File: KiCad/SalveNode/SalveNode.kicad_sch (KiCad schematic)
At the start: 19 parts, among them IC2 TMP75AQDGKRQ1, IC3 DS89C21TMX_NOPB, IC3 VEML7700-TR, J1 Screw_Terminal_01x06, J21 Screw_Terminal_01x06, U1 ATmega328PB-A, Y1 Crystal

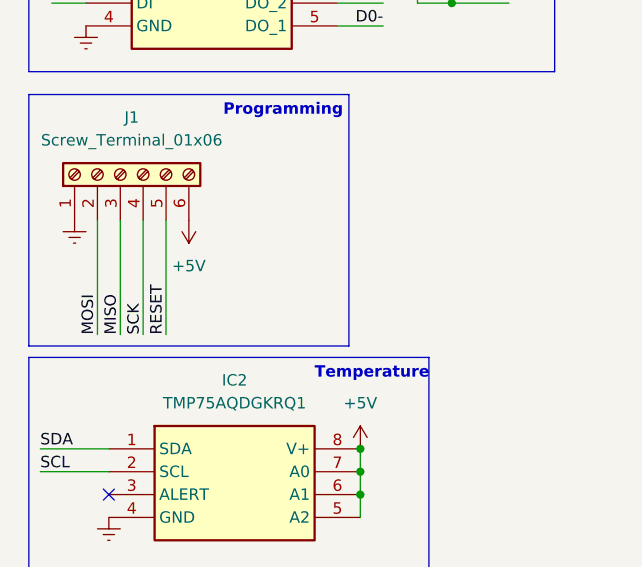
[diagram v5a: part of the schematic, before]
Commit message: fixed missing R for reset while programming
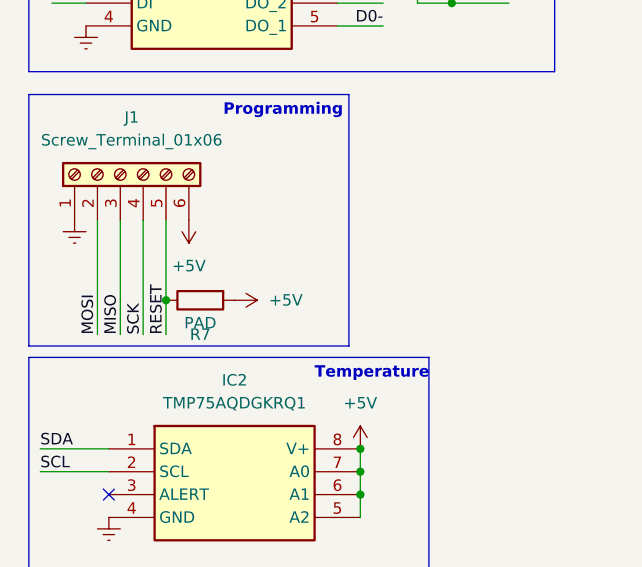
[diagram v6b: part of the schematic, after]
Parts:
- added R7: PAD, Resistor_SMD:R_1206_3216Metric_Pad1.30x1.75mm_HandSolder, symbol Device:R
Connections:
- net +5V: now also R7.2
- net RESET: now also R7.1
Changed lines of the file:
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@@
   (junction (at 156.21 27.94) (diameter 0) (color 0 0 0 0)
+  )
+  (junction (at 30.48 92.71) (diameter 0) (color 0 0 0 0)
   )
   (junction (at 181.61 27.94) (diameter 0) (color 0 0 0 0)
@@
     (stroke (width 0) (type default))
   )
-  (wire (pts (xy 30.48 83.82) (xy 30.48 96.52))
+  (wire (pts (xy 30.48 83.82) (xy 30.48 92.71))
     (stroke (width 0) (type default))
   )
@@
   )
   (wire (pts (xy 25.4 83.82) (xy 25.4 96.52))
+    (stroke (width 0) (type default))
+  )
+  (wire (pts (xy 30.48 92.71) (xy 30.48 96.52))
     (stroke (width 0) (type default))
   )
@@
     )
   )
+  (symbol (lib_id "Device:R") (at 34.29 92.71 90) (mirror x) (unit 1)
+    (in_bom yes) (on_board yes) (dnp no)
+    (property "Reference" "R7" (at 34.29 96.52 90)
+      (effects (font (size 1.27 1.27)))
+    )
+    (property "Value" "PAD" (at 34.29 95.25 90)
+      (effects (font (size 1.27 1.27)))
+    )
+    (property "Footprint" "Resistor_SMD:R_1206_3216Metric_Pad1.30x1.75mm_HandSolder" (at 34.29 90.932 90)
+      (effects (font (size 1.27 1.27)) hide)
+    )
+    (property "Datasheet" "~" (at 34.29 92.71 0)
+      (effects (font (size 1.27 1.27)) hide)
+    )
+    (pin "1")
+    (pin "2")
+    (instances
+      (project "KiCad"
+        (path "/557850ac-a946-4dff-8187-8978353577df"
+          (reference "R7") (unit 1)
+        )
+      )
+      (project "SalveNode"
+        (path "/947c7390-073c-40c7-ae18-83309c4a488f"
+          (reference "R6") (unit 1)
+        )
+      )
+    )
+  )
   (symbol (lib_id "Device:C") (at 168.91 24.13 180) (unit 1)
     (in_bom yes) (on_board yes) (dnp no) (fields_autoplaced)
@@
         )
       )
+    )
+  )
+  (symbol (lib_name "+5V_3") (lib_id "power:+5V") (at 38.1 92.71 270) (unit 1)
+    (in_bom yes) (on_board yes) (dnp no) (fields_autoplaced)
+    (property "Reference" "#PWR024" (at 34.29 92.71 0)
+      (effects (font (size 1.27 1.27)) hide)
+    )
+    (property "Value" "+5V" (at 41.91 92.71 90)
+      (effects (font (size 1.27 1.27)) (justify left))
+    )
+    (property "Footprint" "" (at 38.1 92.71 0)
+      (effects (font (size 1.27 1.27)) hide)
+    )
+    (property "Datasheet" "" (at 38.1 92.71 0)
+      (effects (font (size 1.27 1.27)) hide)
+    )
+    (pin "1")
+    (instances
+      (project "KiCad"
+        (path "/557850ac-a946-4dff-8187-8978353577df"
+          (reference "#PWR024") (unit 1)
+        )
+      )
+      (project "SalveNode"
+        (path "/947c7390-073c-40c7-ae18-83309c4a488f"
+          (reference "#PWR012") (unit 1)
+        )
+      )

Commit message: qwer
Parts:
- R1: value R -> 1k
- R2: value R -> 2k
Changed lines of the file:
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@@
       (effects (font (size 1.27 1.27)) (justify left))
     )
-    (property "Value" "R" (at 21.59 149.86 0)
+    (property "Value" "2k" (at 21.59 149.86 0)
       (effects (font (size 1.27 1.27)) (justify left))
     )
@@
       (effects (font (size 1.27 1.27)) (justify left))
     )
-    (property "Value" "R" (at 21.59 138.43 0)
-      (effects (font (size 1.27 1.27)) (justify left))
-    )
+    (property "Value" "1k" (at 21.59 138.43 0)
+      (effects (font (size 1.27 1.27)) (justify left))
+    )

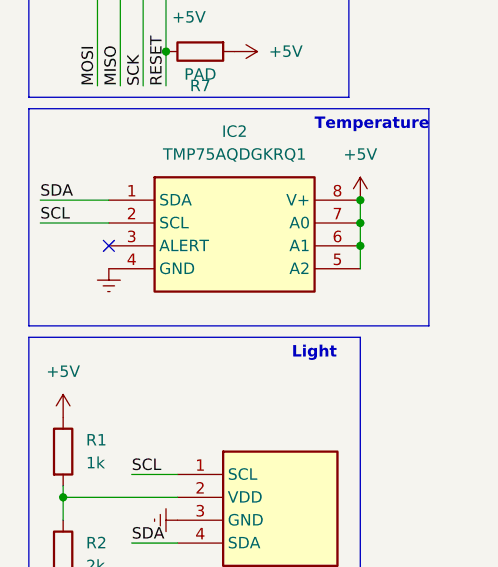
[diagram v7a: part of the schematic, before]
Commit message: Created Arduino Files for Node + fixed missing pullup resistor for ALERT pin in tmp75
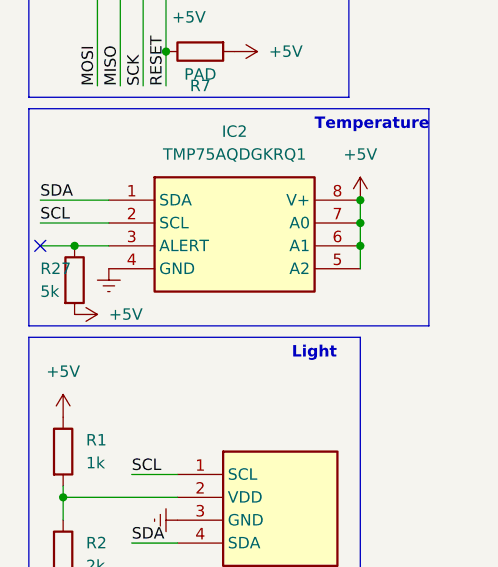
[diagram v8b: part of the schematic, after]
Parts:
- added R27: 5k, Resistor_SMD:R_1206_3216Metric_Pad1.30x1.75mm_HandSolder, symbol Device:R
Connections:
- net +5V: now also R27.2
- net at IC2.3 (ALERT): now also R27.1
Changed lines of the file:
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@@
   (junction (at 52.07 114.3) (diameter 0) (color 0 0 0 0)
+  )
+  (junction (at 20.32 114.3) (diameter 0) (color 0 0 0 0)
   )
   (junction (at 52.07 111.76) (diameter 0) (color 0 0 0 0)
@@
   (no_connect (at 151.13 115.57))
   (no_connect (at 151.13 85.09))
-  (no_connect (at 24.13 114.3))
+  (no_connect (at 16.51 114.3))
   (no_connect (at 151.13 90.17))
   (no_connect (at 181.61 110.49))
@@
     (stroke (width 0) (type default))
   )
+  (wire (pts (xy 16.51 114.3) (xy 20.32 114.3))
+    (stroke (width 0) (type default))
+  )
   (wire (pts (xy 97.79 35.56) (xy 105.41 35.56))
     (stroke (width 0) (type default))
@@
   )
   (wire (pts (xy 166.37 54.61) (xy 166.37 53.34))
+    (stroke (width 0) (type default))
+  )
+  (wire (pts (xy 20.32 114.3) (xy 24.13 114.3))
     (stroke (width 0) (type default))
   )
@@
         (path "/947c7390-073c-40c7-ae18-83309c4a488f"
           (reference "Y1") (unit 1)
+        )
+      )
+    )
+  )
+  (symbol (lib_id "power:+5V") (at 20.32 121.92 270) (unit 1)
+    (in_bom yes) (on_board yes) (dnp no) (fields_autoplaced)
+    (property "Reference" "#PWR013" (at 16.51 121.92 0)
+      (effects (font (size 1.27 1.27)) hide)
+    )
+    (property "Value" "+5V" (at 24.13 121.92 90)
+      (effects (font (size 1.27 1.27)) (justify left))
+    )
+    (property "Footprint" "" (at 20.32 121.92 0)
+      (effects (font (size 1.27 1.27)) hide)
+    )
+    (property "Datasheet" "" (at 20.32 121.92 0)
+      (effects (font (size 1.27 1.27)) hide)
+    )
+    (pin "1")
+    (instances
+      (project "SalveNode"
+        (path "/947c7390-073c-40c7-ae18-83309c4a488f"
+          (reference "#PWR013") (unit 1)
         )
       )
@@
         )
       )
+    )
+  )
+  (symbol (lib_id "Device:R") (at 20.32 118.11 0) (unit 1)
+    (in_bom yes) (on_board yes) (dnp no)
+    (property "Reference" "R27" (at 16.51 116.84 0)
+      (effects (font (size 1.27 1.27)) (justify left))
+    )
+    (property "Value" "5k" (at 16.51 119.38 0)
+      (effects (font (size 1.27 1.27)) (justify left))
+    )
+    (property "Footprint" "Resistor_SMD:R_1206_3216Metric_Pad1.30x1.75mm_HandSolder" (at 18.542 118.11 90)
+      (effects (font (size 1.27 1.27)) hide)
+    )
+    (property "Datasheet" "~" (at 20.32 118.11 0)
+      (effects (font (size 1.27 1.27)) hide)
+    )
+    (pin "1")
+    (pin "2")
+    (instances
+      (project "KiCad"
+        (path "/557850ac-a946-4dff-8187-8978353577df"
+          (reference "R27") (unit 1)
+        )
+      )
+      (project "SalveNode"
+        (path "/947c7390-073c-40c7-ae18-83309c4a488f"
+          (reference "R7") (unit 1)
+        )
+      )
